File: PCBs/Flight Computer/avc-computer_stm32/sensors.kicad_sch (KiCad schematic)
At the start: 12 parts, among them U4 BNO085, U8 BMP581

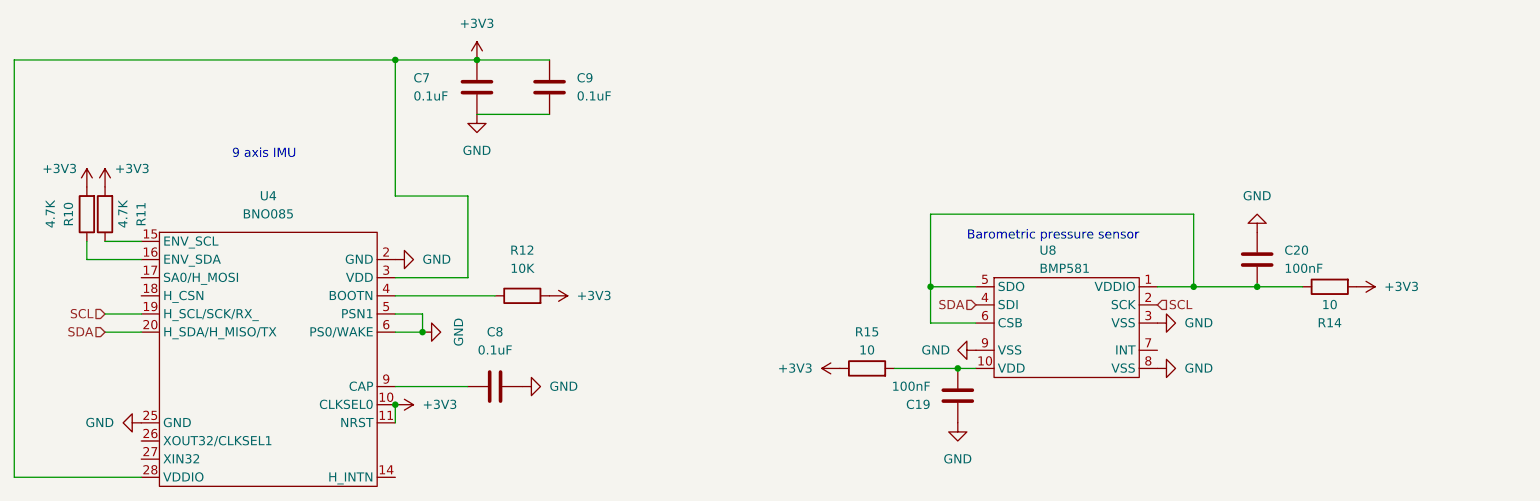
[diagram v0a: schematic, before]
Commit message: Began fixing reference designators
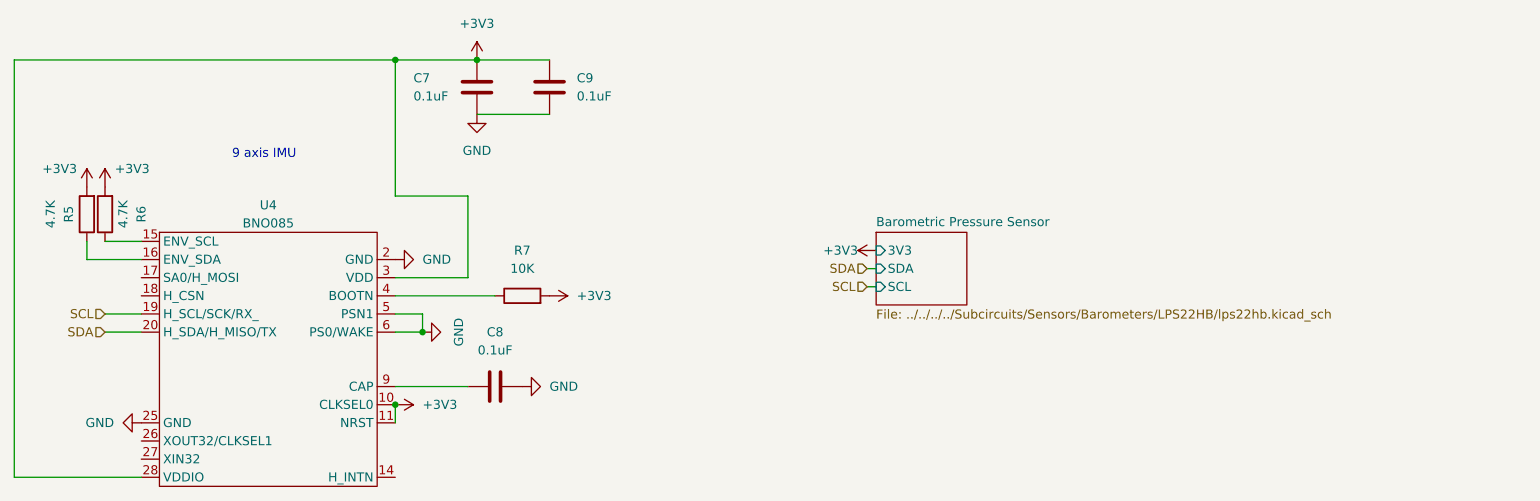
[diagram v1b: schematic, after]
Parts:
- removed C19, C20: 100nF, Capacitor_SMD:C_0805_2012Metric, symbol Device:C
- removed R14, R15: 10, Resistor_SMD:R_0402_1005Metric, symbol Device:R
- removed U8: BMP581, BMP581:BMP581, symbol BMP581:BMP581
- renumbered R10 to R5, R11 to R6, R12 to R7
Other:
- added sheet Barometric Pressure Sensor (../../../../Subcircuits/Sensors/Barometers/LPS22HB/lps22hb.kicad_sch)
- note removed: "Barometric pressure sensor"

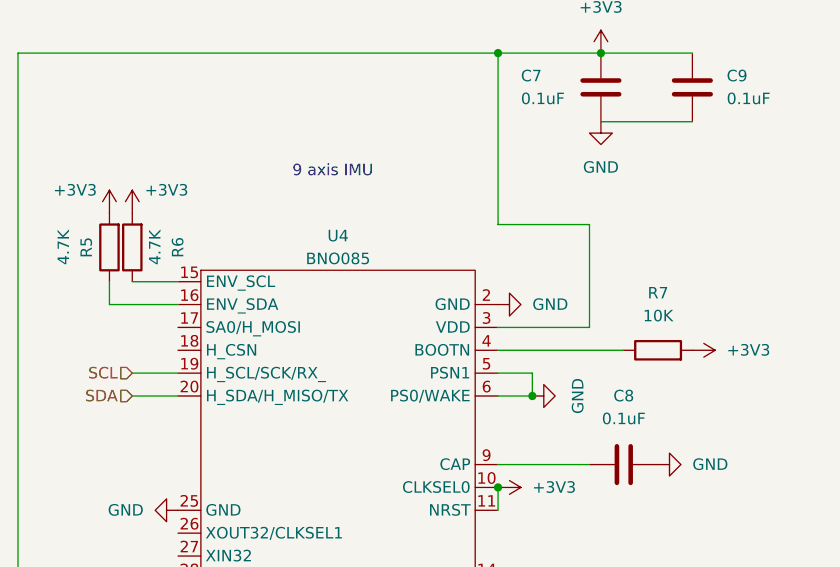
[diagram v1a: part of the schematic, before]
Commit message: Relpaced swithcing regulator with linear regulator. Removed unneccesary components. Replaced barometric pressure sensor with better one. Added connectors for brake servo & hall effect sensor
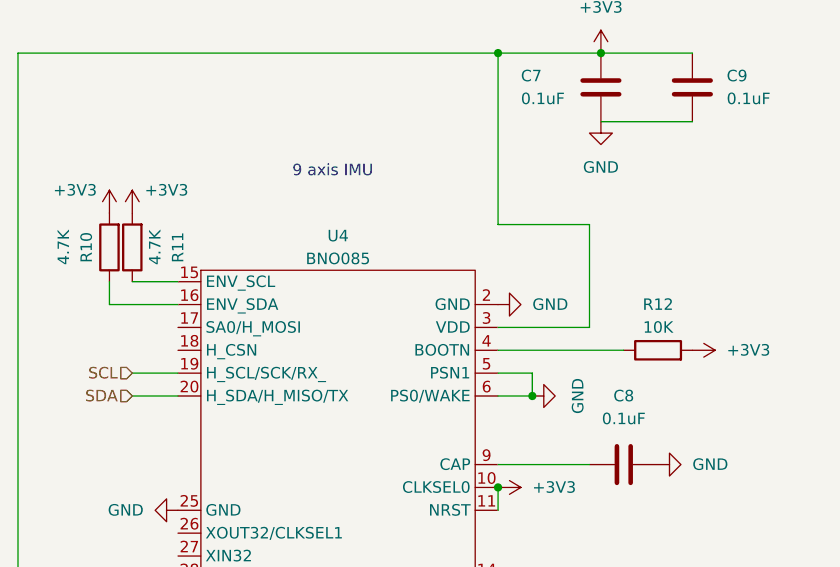
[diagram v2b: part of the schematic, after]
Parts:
- renumbered R5 to R10, R6 to R11, R7 to R12
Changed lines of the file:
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@@
   (symbol (lib_id "Device:R") (at 45.72 64.77 180) (unit 1)
     (in_bom yes) (on_board yes) (dnp no)
-    (property "Reference" "R5" (at 43.18 64.77 90)
+    (property "Reference" "R10" (at 43.18 64.77 90)
       (effects (font (size 1.27 1.27)))
     )
@@
       (project "avc-computer"
         (path "/e63e39d7-6ac0-4ffd-8aa3-1841a4541b55/0097ce40-7767-41a4-a694-1129b95a764c"
-          (reference "R5") (unit 1)
+          (reference "R10") (unit 1)
         )
       )
@@
   (symbol (lib_id "Device:R") (at 106.68 76.2 90) (unit 1)
     (in_bom yes) (on_board yes) (dnp no) (fields_autoplaced)
-    (property "Reference" "R7" (at 106.68 69.85 90)
-      (effects (font (size 1.27 1.27)))
-    )
-    (property "Value" "10K" (at 106.68 72.39 90)
+    (property "Reference" "R12" (at 106.68 71.12 90)
+      (effects (font (size 1.27 1.27)))
+    )
+    (property "Value" "10K" (at 106.68 73.66 90)
       (effects (font (size 1.27 1.27)))
     )
@@
       (project "avc-computer"
         (path "/e63e39d7-6ac0-4ffd-8aa3-1841a4541b55/0097ce40-7767-41a4-a694-1129b95a764c"
-          (reference "R7") (unit 1)
+          (reference "R12") (unit 1)
         )
       )
@@
   (symbol (lib_id "Device:R") (at 48.26 64.77 180) (unit 1)
     (in_bom yes) (on_board yes) (dnp no)
-    (property "Reference" "R6" (at 53.34 64.77 90)
+    (property "Reference" "R11" (at 53.34 64.77 90)
       (effects (font (size 1.27 1.27)))
     )
@@
       (project "avc-computer"
         (path "/e63e39d7-6ac0-4ffd-8aa3-1841a4541b55/0097ce40-7767-41a4-a694-1129b95a764c"
-          (reference "R6") (unit 1)
-        )
-      )
+          (reference "R11") (unit 1)
+        )
+      )

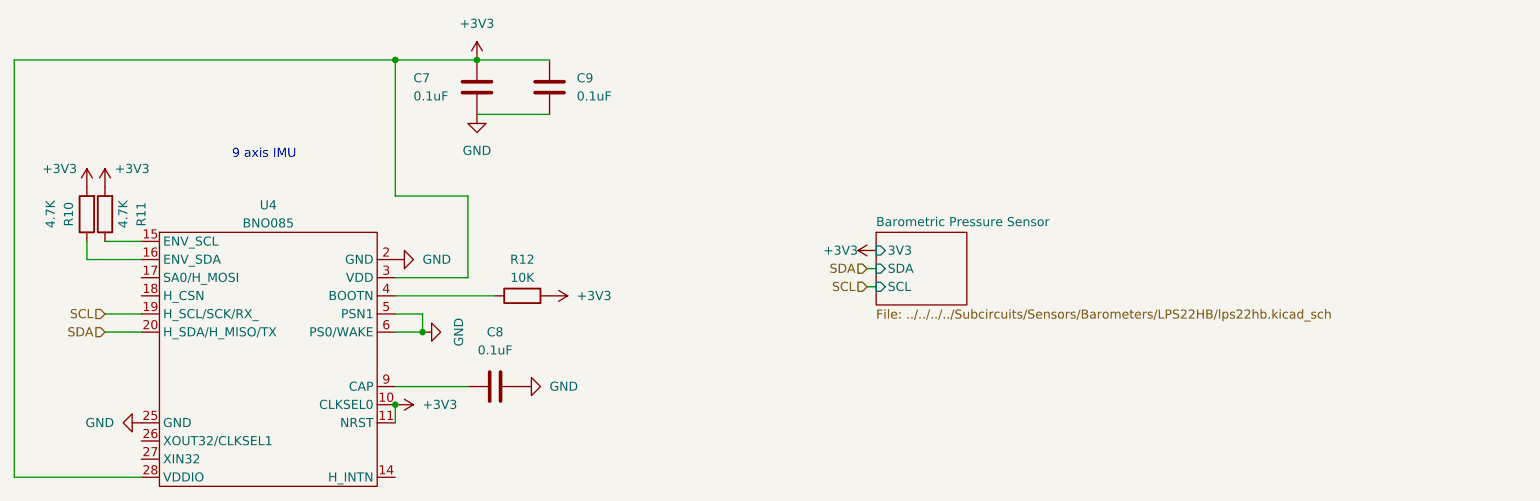
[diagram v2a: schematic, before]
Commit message: Replaced IMU and added 1.9v bus
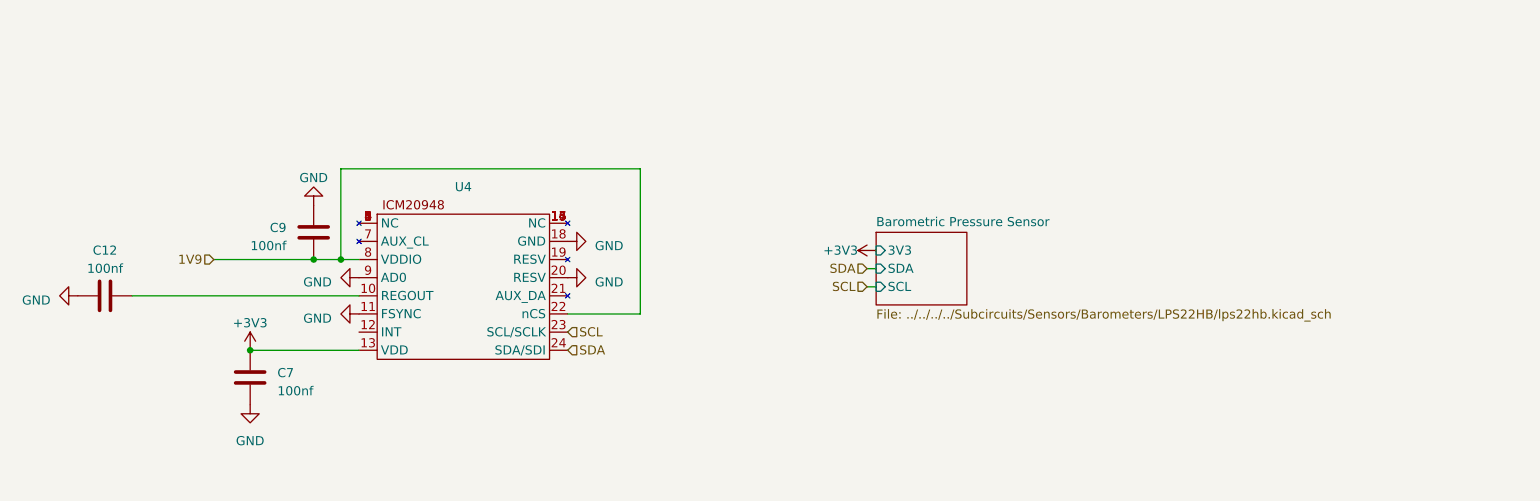
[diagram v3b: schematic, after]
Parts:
- removed C8: 0.1uF, Capacitor_SMD:C_0805_2012Metric, symbol Device:C
- removed R10, R11: 4.7K, Resistor_SMD:R_0805_2012Metric, symbol Device:R
- removed R12: 10K, Resistor_SMD:R_0805_2012Metric, symbol Device:R
- removed U4: BNO085, BNO085:BNO085, symbol BNO085:BNO085
- added C12: 100nf, Capacitor_SMD:C_0805_2012Metric, symbol Device:C
- added U4: ~, Sensor_Motion:InvenSense_QFN-24_3x3mm_P0.4mm, symbol ICM20948:ICM20948
- C7, C9: value 0.1uF -> 100nf
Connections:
- net +3V3: now also U4.13 (VDD); no longer C9.1
- net GND: now also C9.1, C12.1, U4.11 (FSYNC), U4.18 (GND), U4.20 (RESV), U4.9 (AD0); no longer C9.2
- net SCL: now also U4.23 (SCL/SCLK)
- net SDA: now also U4.24 (SDA/SDI)
- new net: U4.1 (NC), U4.2 (NC), U4.3 (NC), U4.4 (NC), U4.5 (NC), U4.6 (NC)
- new net: C12.2, U4.10 (REGOUT)
- new net: U4.14 (NC), U4.15 (NC), U4.16 (NC), U4.17 (NC)
- new net 1V9: C9.2, U4.22 (nCS), U4.8 (VDDIO)
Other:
- note removed: "9 axis IMU"
